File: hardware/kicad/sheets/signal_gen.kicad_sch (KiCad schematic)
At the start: 32 parts, among them U3 SG-8002CA-PH 25MHz, U4 AD9833BRMZ, U5 OPA1656ID, U6 AD633JRZ-R7, U7 MCP4921-E/SN, U8 LM4040DBZ-2.5, U9 OPA188ID

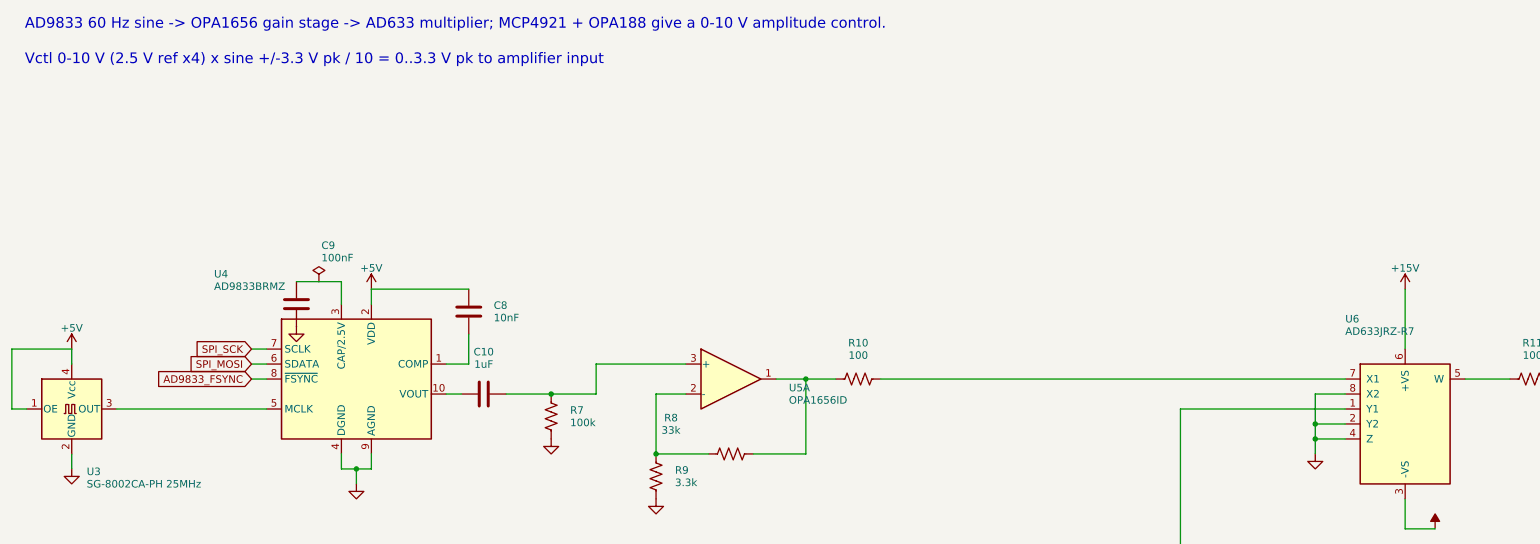
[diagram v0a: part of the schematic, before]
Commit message: Scale sine chain to 10 Vpp full scale and add SPICE sim project
signal_gen: R8 33k -> 51k (OPA1656 gain 11 -> 16.45) so Vctl = 10 V gives
~4.9 V pk (9.9 Vpp, 3.5 Vrms) at SIG_SINE, inside the ZE500.1 RCA input
range (0.2-6 V, from retailer listings, unverified). Schematic note,
DESIGN_REVIEW.md row and schematic PDF updated. ERC 0, 117/117 datasheet
rules, netlist compare shows only the R8 value change.

sim/: separate KiCad project (generated by tools/gen_sim.py) that copies the
analog chain with VSIN/VDC sources in place of the AD9833 and MCP4921, TI
OPA1656/OPA188 models and a behavioural AD633. TI model files are not
committed; see sim/models/README.md.

Co-Authored-By: Claude Sonnet 5.5 <noreply@anthropic.com>
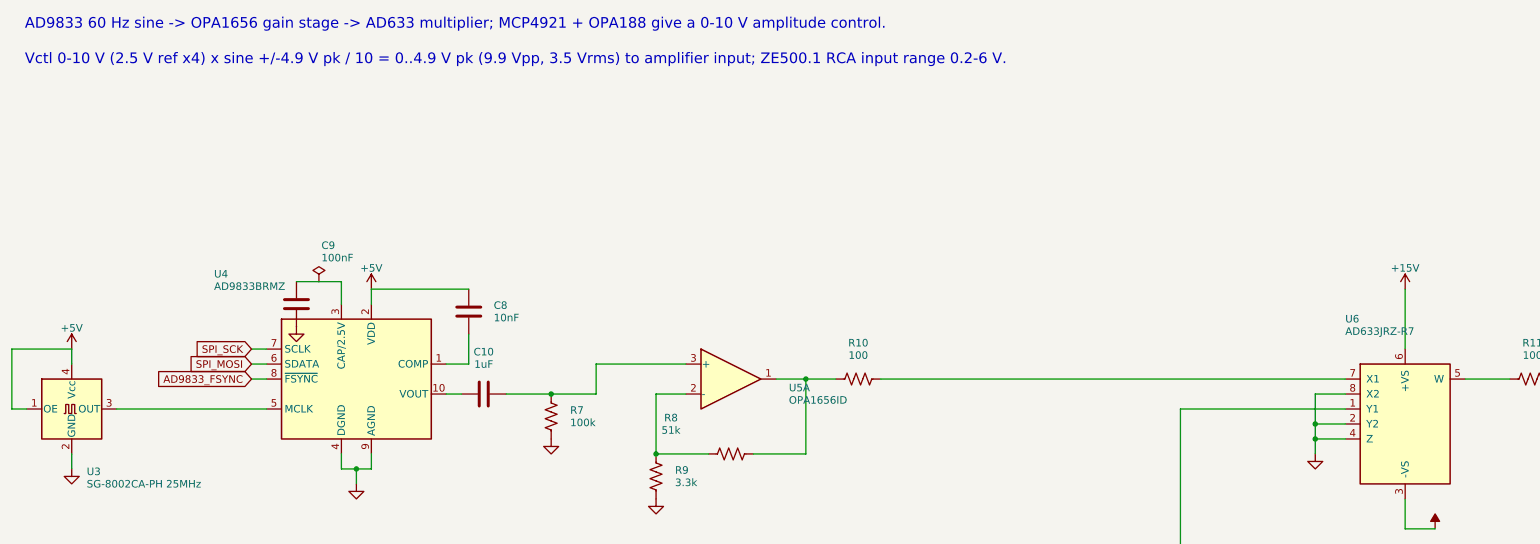
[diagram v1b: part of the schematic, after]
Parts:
- R8: value 33k -> 51k
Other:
- note added: "Vctl 0-10 V (2.5 V ref x4) x sine +/-4.9 V pk / 10 = 0..4.9 V pk (9.9 Vpp, 3.5 Vrms) to amplifier input; ZE500.1 RCA input range 0.2-6 V."
- note removed: "Vctl 0-10 V (2.5 V ref x4) x sine +/-3.3 V pk / 10 = 0..3.3 V pk to amplifier input"
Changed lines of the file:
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@@
 		(company "Cryocooler Controller")
 	)
-	(text "Vctl 0-10 V (2.5 V ref x4) x sine +/-3.3 V pk / 10 = 0..3.3 V pk to amplifier input"
+	(text "Vctl 0-10 V (2.5 V ref x4) x sine +/-4.9 V pk / 10 = 0..4.9 V pk (9.9 Vpp, 3.5 Vrms) to amplifier input; ZE500.1 RCA input range 0.2-6 V."
 		(exclude_from_sim no)
 		(at 20 21 0)
@@
 			)
 		)
-		(property "Value" "33k"
+		(property "Value" "51k"
 			(at 129.54 84.884 270)
 			(show_name no)

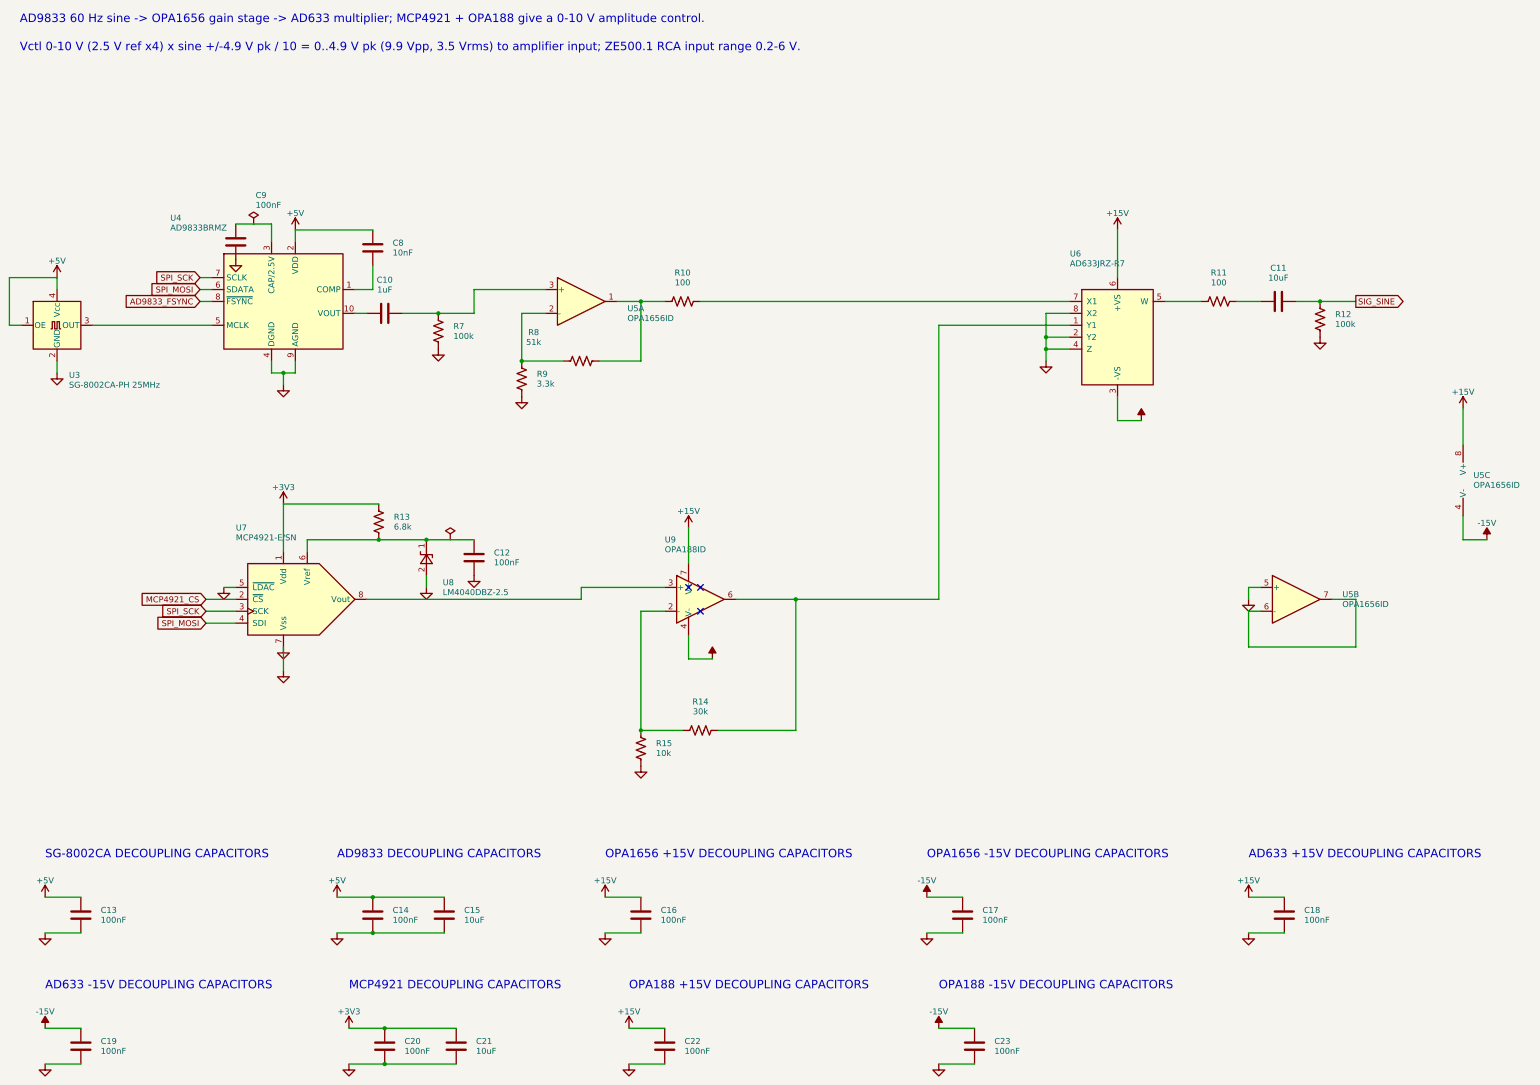
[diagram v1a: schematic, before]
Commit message: Put supply pins on top and grounds on the bottom of IC symbols; flake8-clean Python
Schematic: re-laid out pins on U2, U3, U6, U7, U11, U14, U17-U20, U22-U24
and PS1 (supply on top, ground/strap pins on the bottom edge) via custom
`cryocooler:` symbols (make_lib.from_stock) and a gnd_bus helper; U18/U2
use mirroring instead of a 180 degree rotation. Nets are unchanged (ERC 0,
117/117 datasheet rules, PCB nets still match). Text placement now shows
every power-symbol name, avoids wires, and uses a realistic character width.

Python: black -l 79 -S plus manual wrapping so hardware/kicad and scripts/
pass flake8; add .flake8.

Co-Authored-By: Claude Sonnet 5.5 <noreply@anthropic.com>
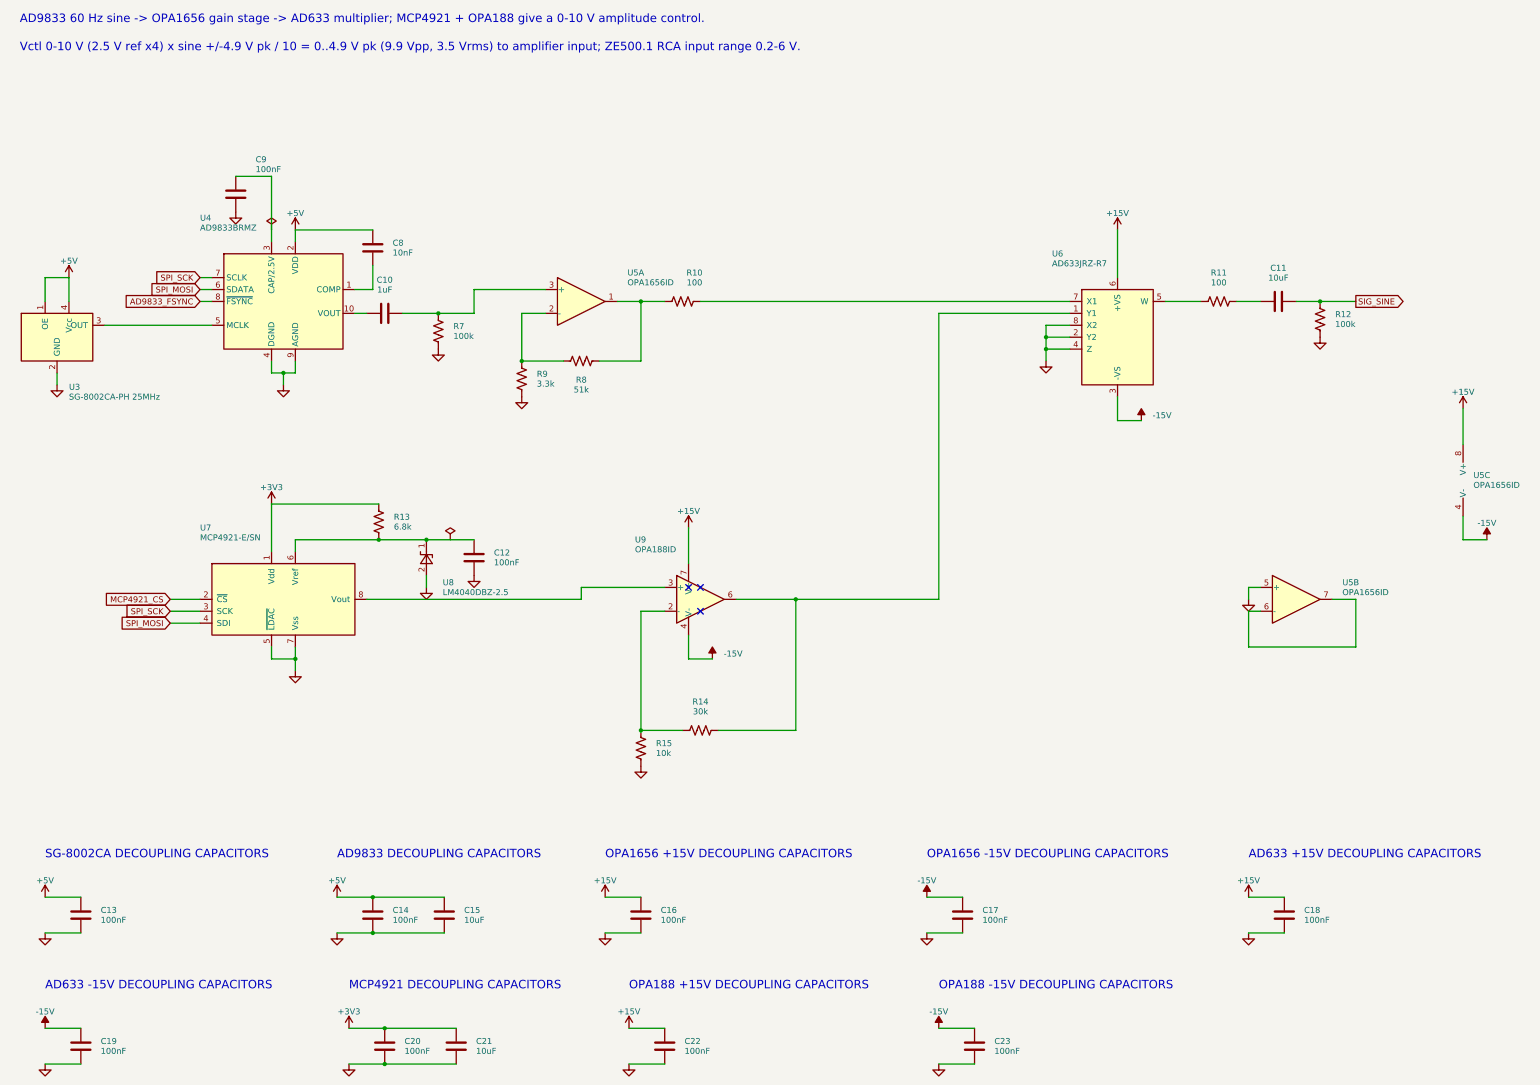
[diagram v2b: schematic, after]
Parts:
- removed R15: 10k, Resistor_SMD:R_0603_1608Metric, symbol Device:R_US
- removed U8: LM4040DBZ-2.5, Package_TO_SOT_SMD:SOT-23, symbol Reference_Voltage:LM4040DBZ-2.5
- added R13: 6.8k, Resistor_SMD:R_0603_1608Metric, symbol Device:R_US
- added U9: OPA188ID, Package_SO:SOIC-8_3.9x4.9mm_P1.27mm, symbol Amplifier_Operational:OPA188xxD
- R15: renamed from U9; value OPA188ID -> 10k; footprint Package_SO:SOIC-8_3.9x4.9mm_P1.27mm -> Resistor_SMD:R_0603_1608Metric; symbol Amplifier_Operational:OPA188xxD -> Device:R_US
- U3: symbol Oscillator:SG-8002CA -> cryocooler:SG-8002CA
- U7: symbol Analog_DAC:MCP4921 -> cryocooler:MCP4921
- U8: renamed from R13; value 6.8k -> LM4040DBZ-2.5; footprint Resistor_SMD:R_0603_1608Metric -> Package_TO_SOT_SMD:SOT-23; symbol Device:R_US -> Reference_Voltage:LM4040DBZ-2.5
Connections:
- net +15V: now also U9.7 (V+); no longer R15.7 (V+)
- net +3V3: now also R13.1; no longer U8.1
- net -15V: now also U9.4 (V-); no longer R15.4 (V-)
- net GND: now also R15.2, U8.2 (A)
- net at C12.1, U7.6 (Vref): now also U8.1 (K), R13.2; no longer U8.2
- net at U7.8 (Vout): now also U9.3 (+); no longer R15.3 (+)
- net at R15.1: now also R14.1, U9.2 (-)
- net at R14.2, U6.1 (Y1): now also U9.6; no longer R15.6
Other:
- moved on the sheet: C9, U8
